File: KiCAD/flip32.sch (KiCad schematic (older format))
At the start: 51 parts, among them CON1 USB-MICRO-B, IC2 MIC5205, P1 VBAT, P10 BOOT, P2 ESC OUT, P3 BEEPER, P4 RECV CHANNELS, P5 UART 1, P6 I2C, P7 UNUSED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

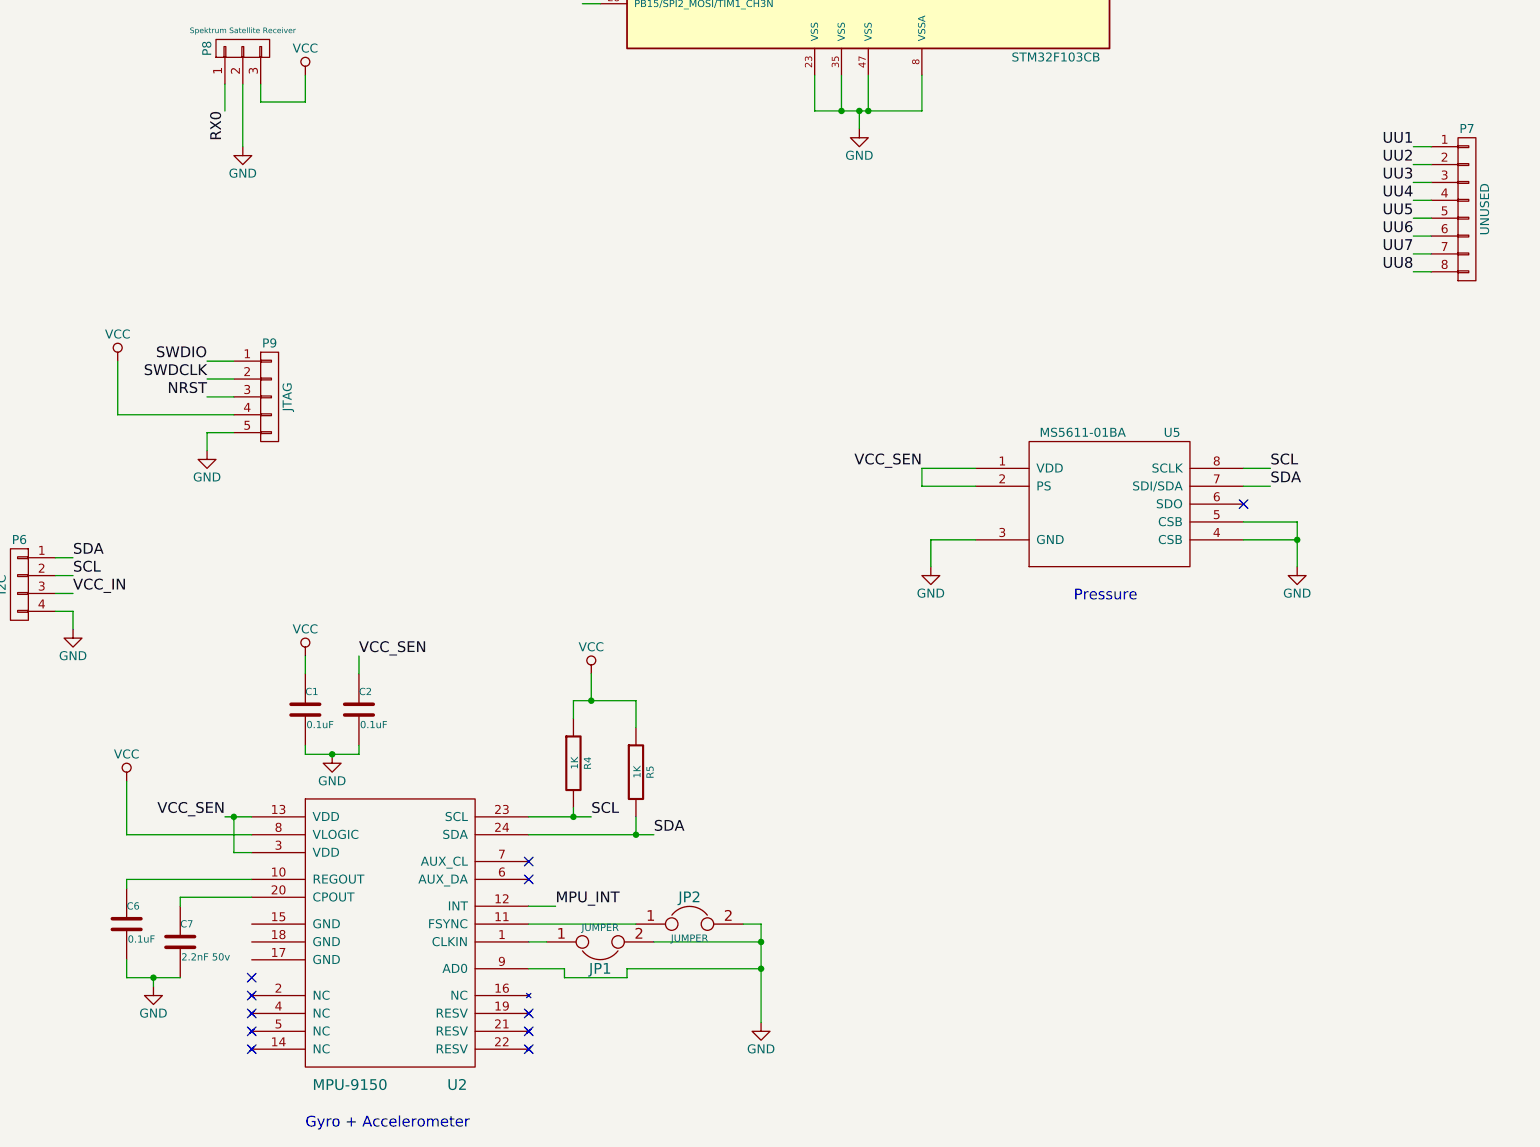
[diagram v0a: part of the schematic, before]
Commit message: swapped from old mpu9150 to newer mpu9250
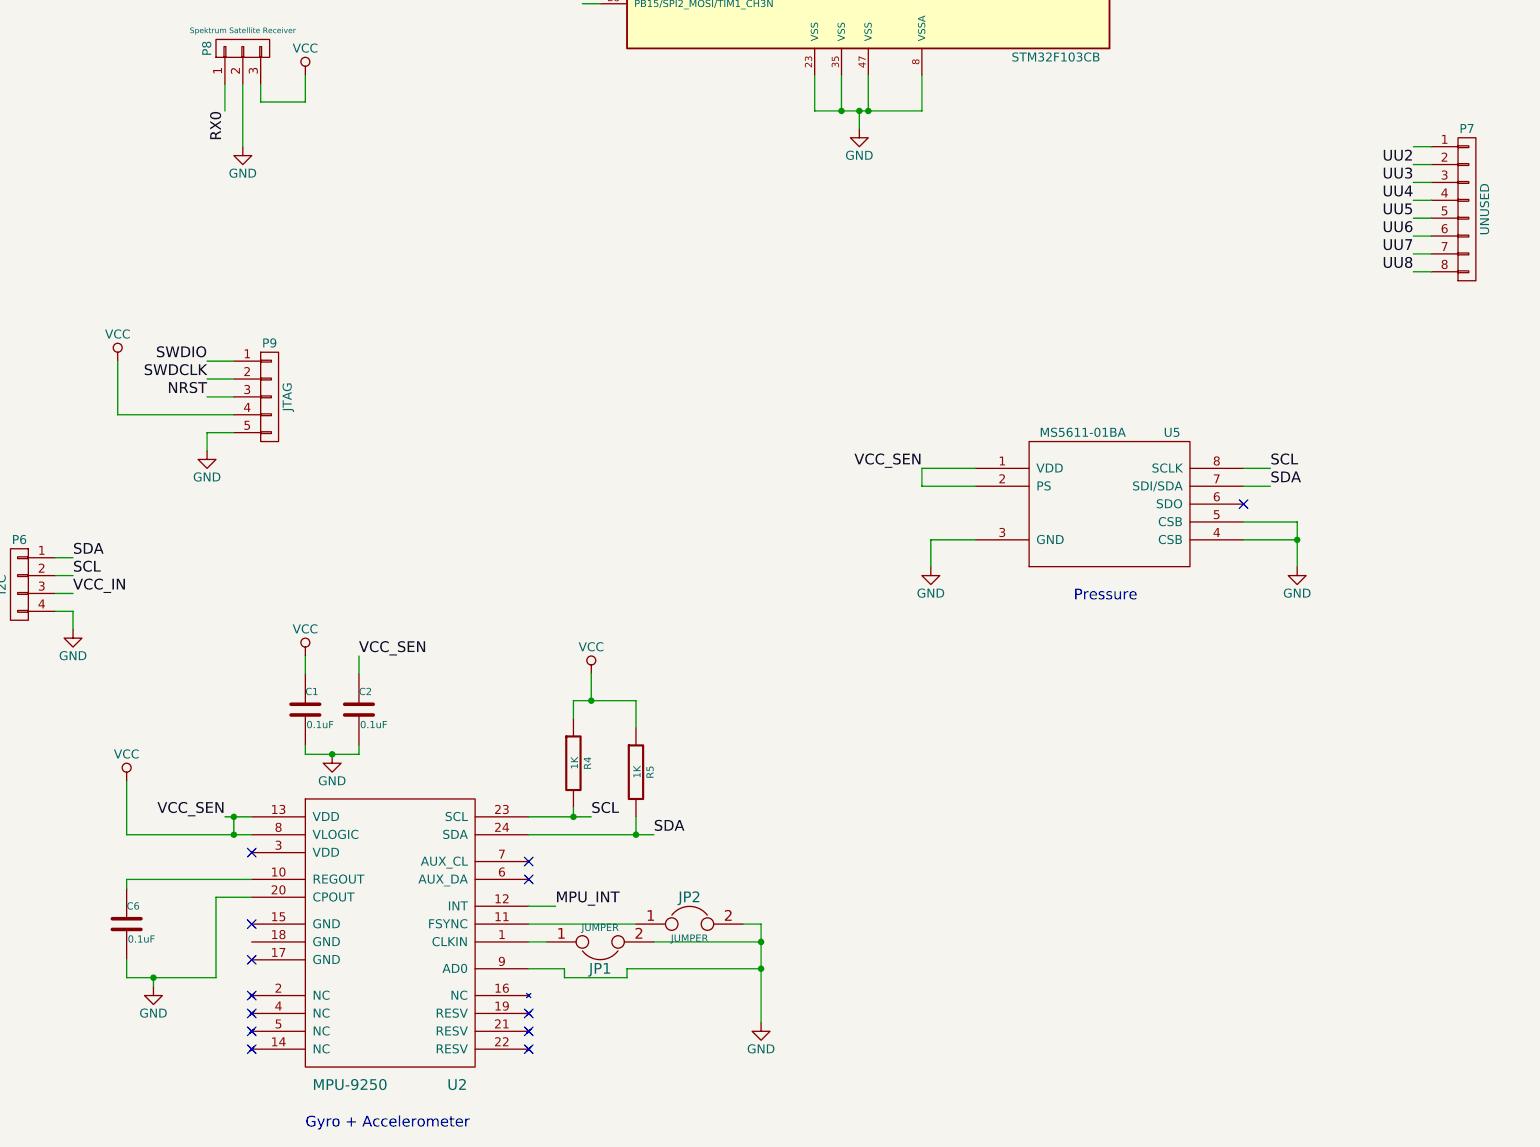
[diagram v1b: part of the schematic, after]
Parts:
- removed C7: 2.2nF 50v, ~, symbol C
- U2: value MPU-9150 -> MPU-9250
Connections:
- net GND: now also U2.20 (CPOUT)
- net VCC: now also C10.1, C11.1, C2.1, IC2.5 (VOUT), U2.13 (VDD), U5.1 (VDD), U5.2 (PS)
- net UU1: no longer names the net of P7.1 (P1)
- removed net VCC_SEN: C10.1, C11.1, C2.1, IC2.5 (VOUT), U2.13 (VDD), U2.3 (VDD), U5.1 (VDD), U5.2 (PS)
- no-connect marks 36 -> 38
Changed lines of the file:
@@
 Sheet 1 1
 Title "Flip32+"
-Date "16 jul 2015"
+Date "20 jul 2015"
 Rev "1"
 Comp ""
@@
 Wire Wire Line
 	14550 1100 14550 1200
-NoConn ~ 5050 9950
 NoConn ~ 5050 10050
 NoConn ~ 5050 10150
@@
 F 3 "" H 7900 10200 60  0000 C CNN
 	1    7900 10200
-	1    0    0    -1
-$EndComp
-$Comp
-L C C7
-U 1 1 559FDE02
-P 4650 9750
-F 0 "C7" H 4650 9850 40  0000 L CNN
-F 1 "2.2nF 50v" H 4656 9665 40  0000 L CNN
-F 2 "~" H 4688 9600 30  0000 C CNN
-F 3 "~" H 4650 9750 60  0000 C CNN
-	1    4650 9750
 	1    0    0    -1
 $EndComp
@@
 P 5850 9850
 F 0 "U2" H 6200 9150 60  0000 C CNN
-F 1 "MPU-9150" H 5600 9150 60  0000 C CNN
+F 1 "MPU-9250" H 5600 9150 60  0000 C CNN
 F 2 "~" H 5850 9600 60  0000 C CNN
 F 3 "~" H 5850 9600 60  0000 C CNN
@@
 $EndComp
 Wire Wire Line
-	4350 9950 4650 9950
+	4350 9950 4850 9950
 Wire Wire Line
 	4500 9950 4500 10000
@@
 Wire Wire Line
 	4350 9400 4350 9450
-Wire Wire Line
-	5050 9500 4650 9500
-Wire Wire Line
-	4650 9500 4650 9550
-Wire Wire Line
-	5050 9250 4950 9250
-Wire Wire Line
-	4950 9250 4950 9050
 Connection ~ 4950 9050
 $Comp
@@
 Wire Wire Line
 	6900 4500 7000 4500
-Text Label 11550 5300 2    60   ~ 0
-UU1
 Text Label 11550 5400 2    60   ~ 0
 UU2
@@
 Text Label 10100 3050 0    60   ~ 0
 BEEP
+Wire Wire Line
+	4950 9150 4950 9050
+Connection ~ 4950 9150
+NoConn ~ 5050 9250
+NoConn ~ 5050 9850
+NoConn ~ 5050 9650
+Wire Wire Line
+	5050 9500 4850 9500
+Wire Wire Line
+	4850 9500 4850 9950
 $EndSCHEMATC

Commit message: add renders of board
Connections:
- net VCC: no longer C10.1, C11.1, C2.1, IC2.5 (VOUT), U2.13 (VDD), U5.1 (VDD), U5.2 (PS)
- new net VCC_SEN: C10.1, C11.1, C2.1, IC2.5 (VOUT), U2.13 (VDD), U5.1 (VDD), U5.2 (PS)
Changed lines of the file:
@@
 	5050 9050 4900 9050
-Wire Wire Line
-	5050 9150 4350 9150
 Wire Wire Line
 	4350 9150 4350 8850
@@
 Wire Wire Line
 	4350 9400 4350 9450
-Connection ~ 4950 9050
 $Comp
 L JUMPER JP2
@@
 Text Label 10100 3050 0    60   ~ 0
 BEEP
-Wire Wire Line
-	4950 9150 4950 9050
-Connection ~ 4950 9150
 NoConn ~ 5050 9250
 NoConn ~ 5050 9850
@@
 Wire Wire Line
 	4850 9500 4850 9950
+Wire Wire Line
+	5050 9150 4350 9150
 $EndSCHEMATC
